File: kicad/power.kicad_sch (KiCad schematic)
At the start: 6 parts, among them J1 Bus_PCI_Express_x1, J6 USB_C_Receptacle_USB2.0_16P

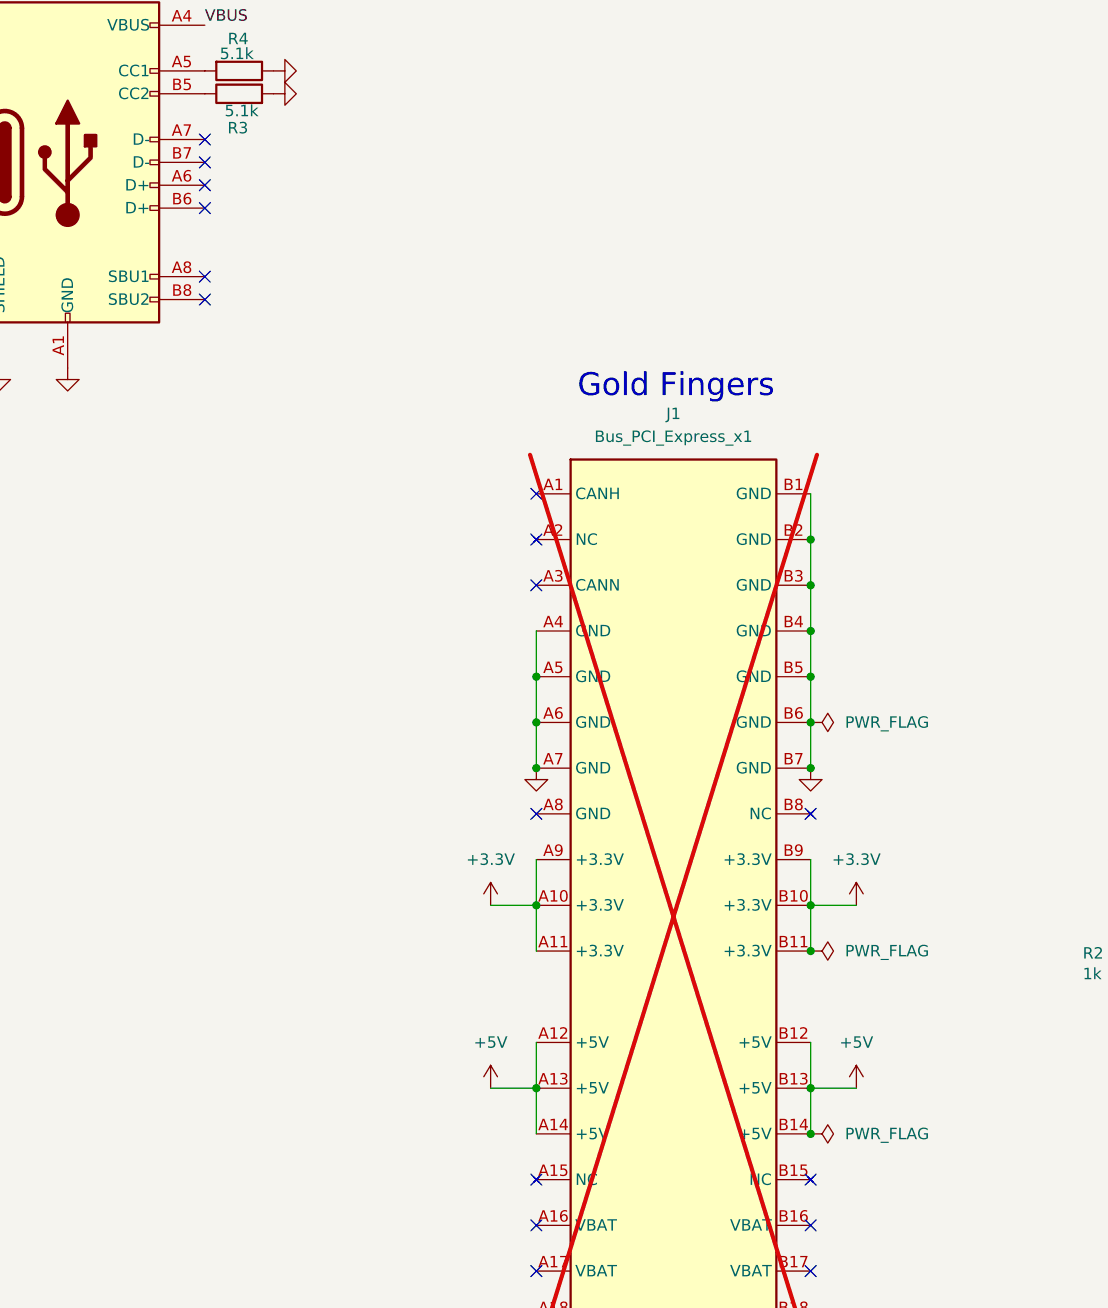
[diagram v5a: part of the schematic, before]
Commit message: update symbol data fields, add lcsc PN and links
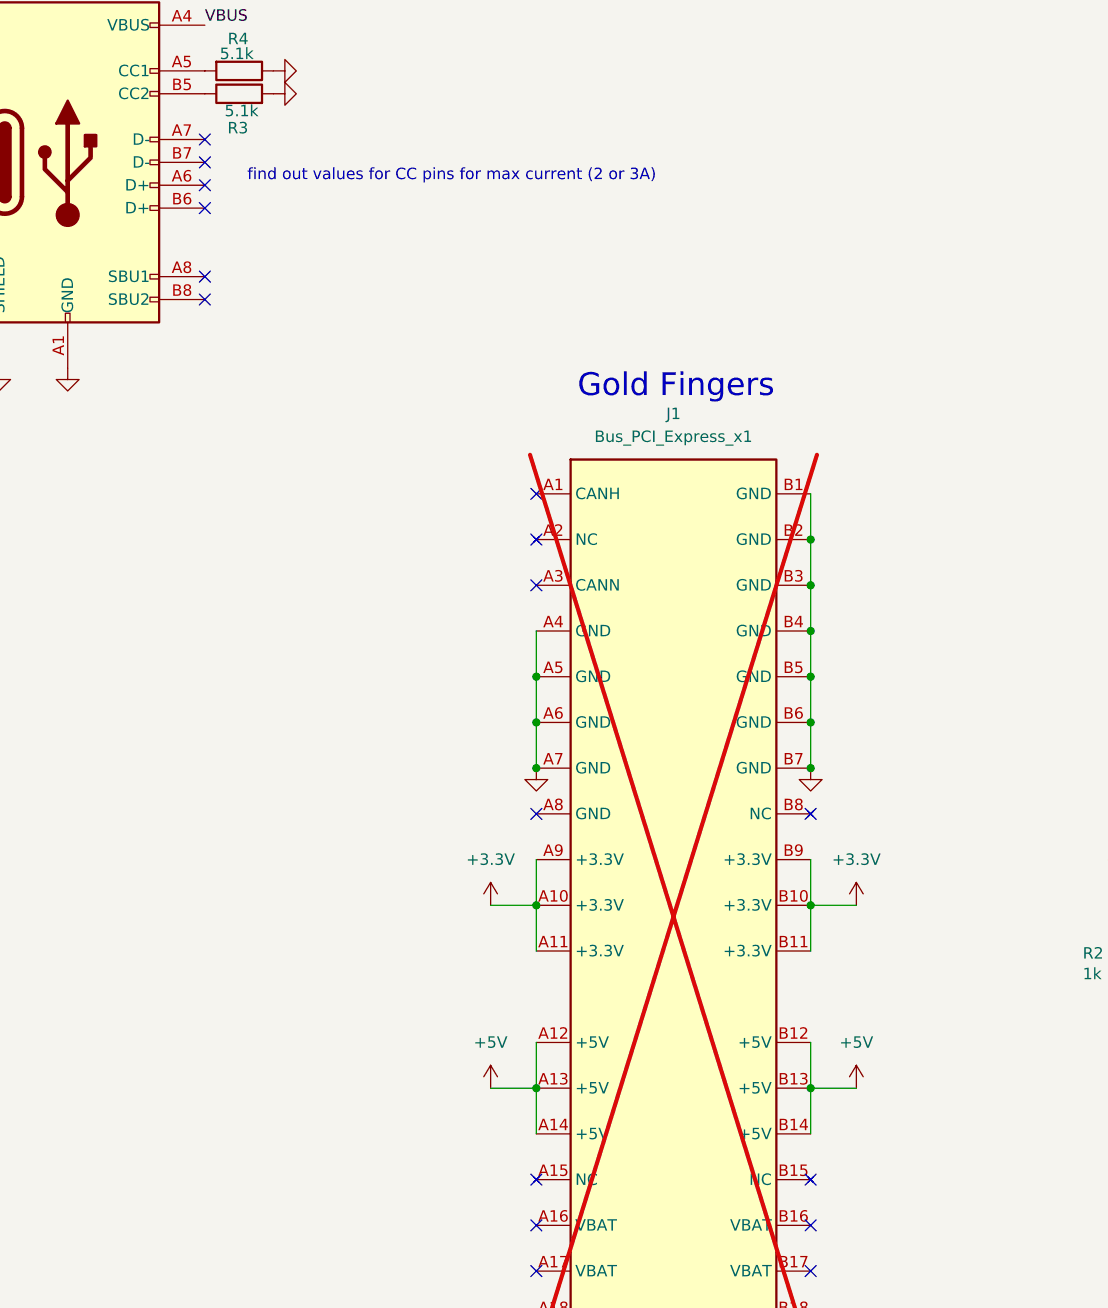
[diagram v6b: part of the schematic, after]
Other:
- note added: "find out values for CC pins for max current (2 or 3A)"

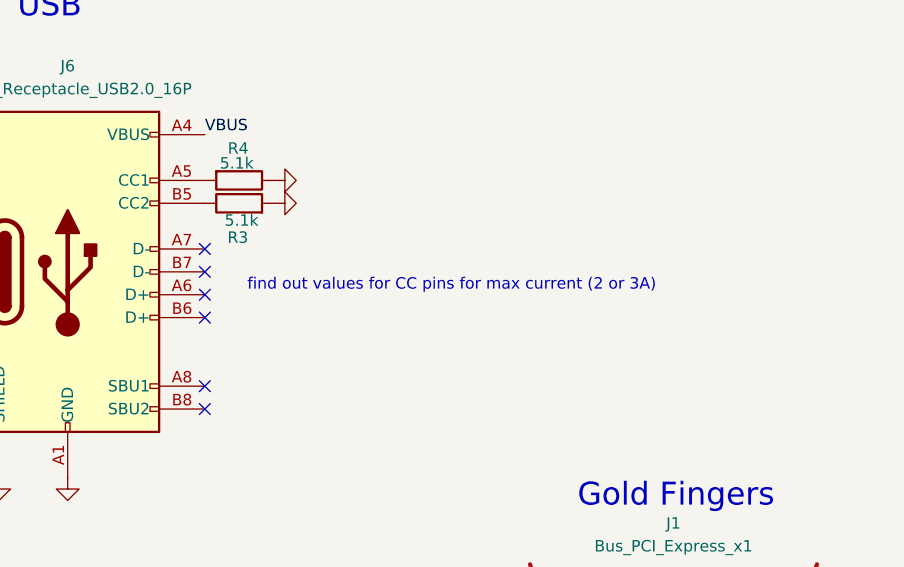
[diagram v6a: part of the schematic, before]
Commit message: delete old buck, replace with buck/boost
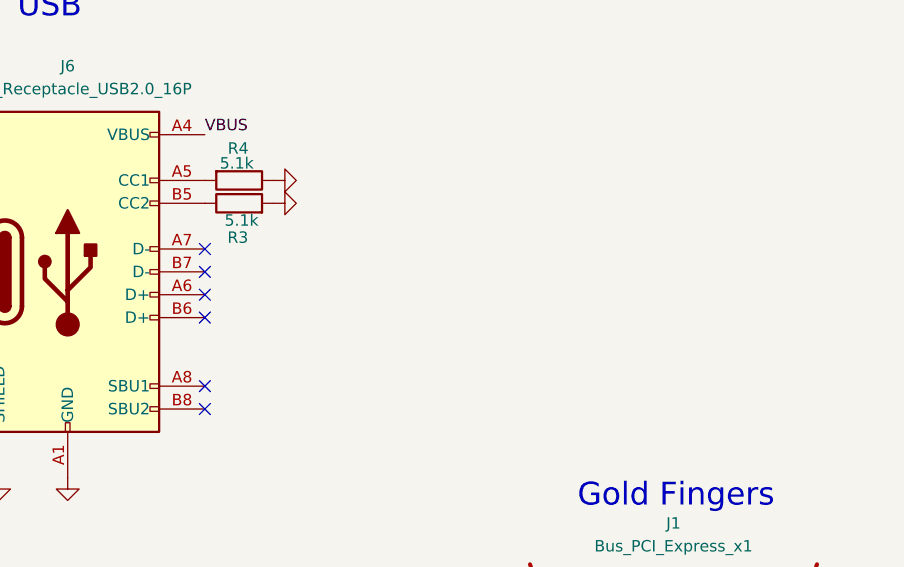
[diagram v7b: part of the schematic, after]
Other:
- note removed: "find out values for CC pins for max current (2 or 3A)"
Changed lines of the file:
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@@
-		)
-	)
-	(text "find out values for CC pins for max current (2 or 3A)"
-		(exclude_from_sim no)
-		(at 82.042 54.864 0)
-		(effects
-			(font
-				(size 1.27 1.27)
-			)
 		)
 	)

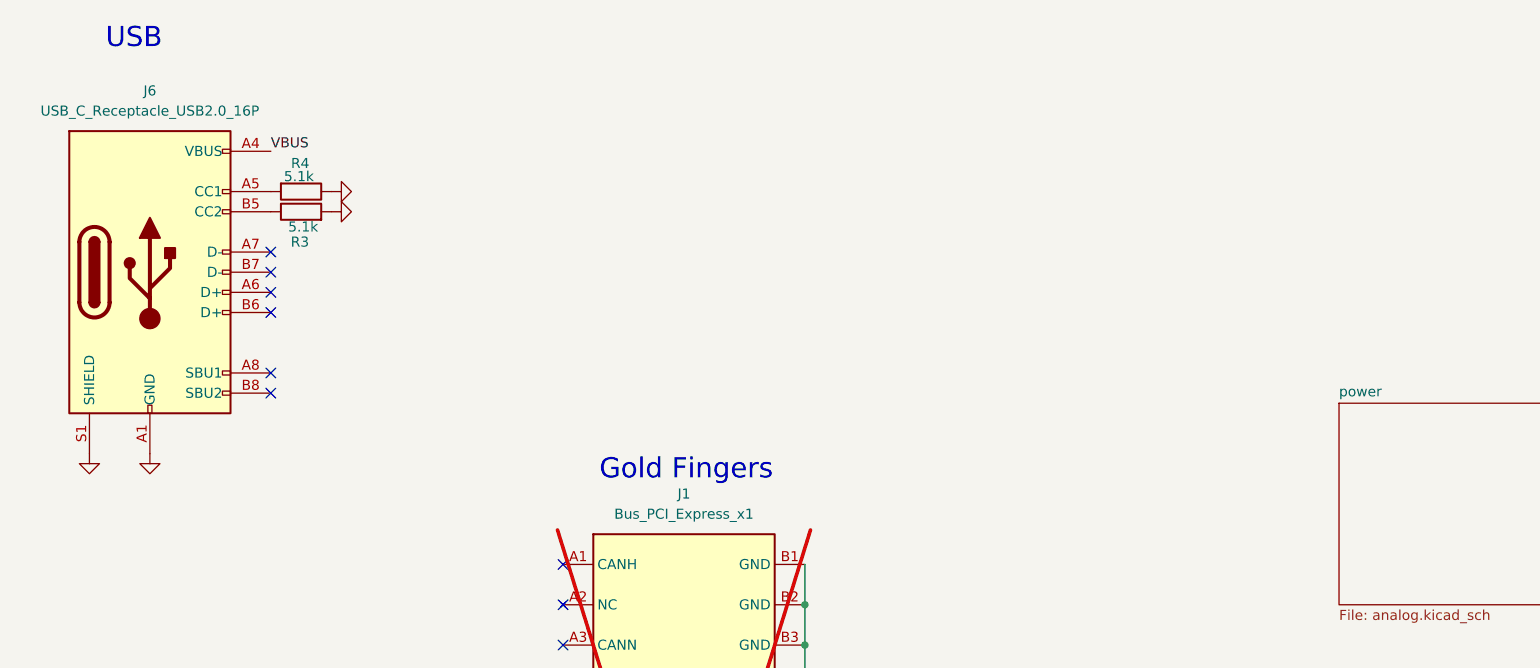
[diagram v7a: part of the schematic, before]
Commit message: add 5v buck-boost schematic
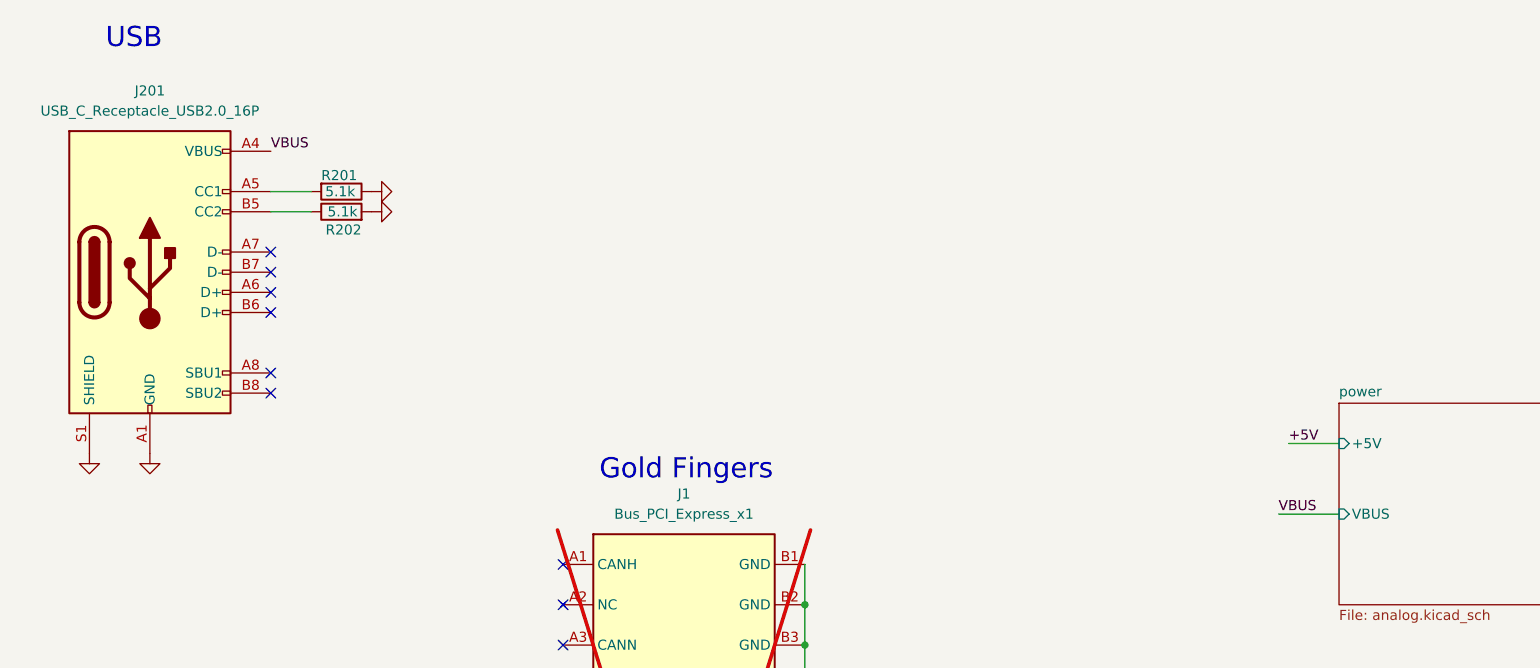
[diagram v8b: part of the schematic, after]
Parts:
- renumbered J6 to J201, R4 to R201, R3 to R202
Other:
- sheet power ports: added +5V, VBUS; removed none
- moved on the sheet: R201, R202
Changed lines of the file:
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@@
+	(wire
+		(pts
+			(xy 59.69 43.18) (xy 54.61 43.18)
+		)
+		(stroke
+			(width 0)
+			(type default)
+		)
+	)
 	(wire
 		(pts
@@
 	(wire
 		(pts
+			(xy 181.61 83.82) (xy 189.23 83.82)
+		)
+		(stroke
+			(width 0)
+			(type default)
+		)
+	)
+	(wire
+		(pts
 			(xy 86.36 135.89) (xy 91.44 135.89)
 		)
@@
 	(wire
 		(pts
+			(xy 182.88 74.93) (xy 189.23 74.93)
+		)
+		(stroke
+			(width 0)
+			(type default)
+		)
+	)
+	(wire
+		(pts
 			(xy 91.44 115.57) (xy 91.44 120.65)
 		)
@@
 	(wire
 		(pts
+			(xy 59.69 45.72) (xy 54.61 45.72)
+		)
+		(stroke
+			(width 0)
+			(type default)
+		)
+	)
+	(wire
+		(pts
 			(xy 91.44 156.21) (xy 91.44 151.13)
 		)
@@
 			(width 0)
 			(type default)
+		)
+	)
+	(label "+5V"
+		(at 182.88 74.93 0)
+		(effects
+			(font
+				(size 1.27 1.27)
+			)
+			(justify left bottom)
 		)
 	)
 	(label "VBUS"
 		(at 54.61 38.1 0)
+		(effects
+			(font
+				(size 1.27 1.27)
+			)
+			(justify left bottom)
+		)
+	)
+	(label "VBUS"
+		(at 181.61 83.82 0)
 		(effects
 			(font
@@
 	(symbol
 		(lib_id "power:GND")
-		(at 62.23 45.72 90)
+		(at 67.31 45.72 90)
 		(unit 1)
 		(exclude_from_sim no)
@@
 		(fields_autoplaced yes)
 		(property "Reference" "#PWR019"
-			(at 68.58 45.72 0)
+			(at 73.66 45.72 0)
 			(effects
 				(font
@@
 		)
 		(property "Value" "GND"
+			(at 72.39 45.72 0)
+			(effects
+				(font
+					(size 1.27 1.27)
+				)
+				(hide yes)
+			)
+		)
+		(property "Footprint" ""
 			(at 67.31 45.72 0)
 			(effects
@@
 			)
 		)
-		(property "Footprint" ""
-			(at 62.23 45.72 0)
-			(effects
-				(font
-					(size 1.27 1.27)
-				)
-				(hide yes)
-			)
-		)
 		(property "Datasheet" ""
-			(at 62.23 45.72 0)
+			(at 67.31 45.72 0)
 			(effects
 				(font
@@
 		)
 		(property "Description" "Power symbol creates a global label with name \"GND\" , ground"
-			(at 62.23 45.72 0)
+			(at 67.31 45.72 0)
 			(effects
 				(font
@@
 	(symbol
 		(lib_id "power:GND")
-		(at 62.23 43.18 90)
+		(at 67.31 43.18 90)
 		(unit 1)
 		(exclude_from_sim no)
@@
 		(fields_autoplaced yes)
 		(property "Reference" "#PWR020"
-			(at 68.58 43.18 0)
+			(at 73.66 43.18 0)
 			(effects
 				(font
@@
 		)
 		(property "Value" "GND"
+			(at 72.39 43.18 0)
+			(effects
+				(font
+					(size 1.27 1.27)
+				)
+				(hide yes)
+			)
+		)
+		(property "Footprint" ""
 			(at 67.31 43.18 0)
 			(effects
@@
 			)
 		)
-		(property "Footprint" ""
-			(at 62.23 43.18 0)
-			(effects
-				(font
-					(size 1.27 1.27)
-				)
-				(hide yes)
-			)
-		)
 		(property "Datasheet" ""
-			(at 62.23 43.18 0)
+			(at 67.31 43.18 0)
 			(effects
 				(font
@@
 		)
 		(property "Description" "Power symbol creates a global label with name \"GND\" , ground"
-			(at 62.23 43.18 0)
+			(at 67.31 43.18 0)
 			(effects
 				(font
@@
 	(symbol
 		(lib_id "Device:R")
-		(at 58.42 45.72 90)
+		(at 63.5 45.72 90)
 		(unit 1)
 		(exclude_from_sim no)
@@
 		(on_board yes)
 		(dnp no)
-		(property "Reference" "R3"
-			(at 59.436 49.53 90)
+		(property "Reference" "R202"
+			(at 66.04 48.006 90)
 			(effects
 				(font
@@
 		)
 		(property "Value" "5.1k"
-			(at 60.579 47.625 90)
+			(at 65.532 45.72 90)
 			(effects
 				(font
@@
 		)
 		(property "Footprint" "Resistor_SMD:R_0402_1005Metric"
-			(at 58.42 47.498 90)
+			(at 63.5 47.498 90)
 			(effects
 				(font
@@
 		)
 		(property "Datasheet" "~"
-			(at 58.42 45.72 0)
+			(at 63.5 45.72 0)
 			(effects
 				(font
@@
 		)
 		(property "Description" "Resistor"
-			(at 58.42 45.72 0)
+			(at 63.5 45.72 0)
 			(effects
 				(font
@@
 		)
 		(property "JLC Link" "https://jlcpcb.com/partdetail/26648-0402WGF5101TCE/C25905"
-			(at 58.42 45.72 0)
+			(at 63.5 45.72 0)
 			(effects
 				(font
@@
 		)
 		(property "basic?" "yes"
-			(at 58.42 45.72 0)
+			(at 63.5 45.72 0)
 			(effects
 				(font
@@
 		)
 		(property "info" "5.1k ohm"
-			(at 58.42 45.72 0)
+			(at 63.5 45.72 0)
 			(effects
 				(font
@@
 		)
 		(property "price" "C$0.0006"
-			(at 58.42 45.72 0)
+			(at 63.5 45.72 0)
 			(effects
 				(font
@@
 		)
 		(property "notes" ""
-			(at 58.42 45.72 0)
+			(at 63.5 45.72 0)
 			(effects
 				(font
@@
 		)
 		(property "LCSC PN" "C25905"
-			(at 58.42 45.72 0)
+			(at 63.5 45.72 0)
 			(effects
 				(font
@@
 		)
 		(property "Package" ""
-			(at 58.42 45.72 90)
+			(at 63.5 45.72 90)
 			(effects
 				(font
@@
 		)
 		(property "Comment" ""
-			(at 58.42 45.72 90)
+			(at 63.5 45.72 90)
 			(effects
 				(font
@@
 		)
 		(property "Current Draw" ""
-			(at 58.42 45.72 90)
+			(at 63.5 45.72 90)
 			(effects
 				(font
@@
 		)
 		(property "TYPE" ""
-			(at 58.42 45.72 90)
+			(at 63.5 45.72 90)
 			(effects
 				(font
@@
 			(project "sensors"
 				(path "/612ece3f-e722-4b33-8111-645d24cfcf05"
-					(reference "R3")
+					(reference "R202")
 					(unit 1)
 				)
@@
 	(symbol
 		(lib_id "Device:R")
-		(at 58.42 43.18 270)
+		(at 63.5 43.18 270)
 		(unit 1)
 		(exclude_from_sim no)
@@
 		(on_board yes)
 		(dnp no)
-		(property "Reference" "R4"
-			(at 57.15 39.624 90)
+		(property "Reference" "R201"
+			(at 60.96 41.148 90)
 			(effects
 				(font
@@
 		)
 		(property "Value" "5.1k"
-			(at 56.261 41.275 90)
+			(at 61.468 43.18 90)
 			(effects
 				(font
@@
 		)
 		(property "Footprint" "Resistor_SMD:R_0402_1005Metric"
-			(at 58.42 41.402 90)
+			(at 63.5 41.402 90)
 			(effects
 				(font
@@
 		)
 		(property "Datasheet" "~"
-			(at 58.42 43.18 0)
+			(at 63.5 43.18 0)
 			(effects
 				(font
@@
 		)
 		(property "Description" "Resistor"
-			(at 58.42 43.18 0)
+			(at 63.5 43.18 0)
 			(effects
 				(font
@@
 		)
 		(property "JLC Link" "https://jlcpcb.com/partdetail/26648-0402WGF5101TCE/C25905"
-			(at 58.42 43.18 0)
+			(at 63.5 43.18 0)
 			(effects
 				(font
@@
 		)
 		(property "basic?" "yes"
-			(at 58.42 43.18 0)
+			(at 63.5 43.18 0)
 			(effects
 				(font
@@
 		)
 		(property "info" "5.1k ohm"
-			(at 58.42 43.18 0)
+			(at 63.5 43.18 0)
 			(effects
 				(font
@@
 		)
 		(property "price" "C$0.0006"
-			(at 58.42 43.18 0)
+			(at 63.5 43.18 0)
 			(effects
 				(font
@@
 		)
 		(property "notes" ""
-			(at 58.42 43.18 0)
+			(at 63.5 43.18 0)
 			(effects
 				(font
@@
 		)
 		(property "LCSC PN" "C25905"
-			(at 58.42 43.18 0)
+			(at 63.5 43.18 0)
 			(effects
 				(font
@@
 		)
 		(property "Package" ""
-			(at 58.42 43.18 90)
+			(at 63.5 43.18 90)
 			(effects
 				(font
@@
 		)
 		(property "Comment" ""
-			(at 58.42 43.18 90)
+			(at 63.5 43.18 90)
 			(effects
 				(font
@@
 		)
 		(property "Current Draw" ""
-			(at 58.42 43.18 90)
+			(at 63.5 43.18 90)
 			(effects
 				(font
@@
 		)
 		(property "TYPE" ""
-			(at 58.42 43.18 90)
+			(at 63.5 43.18 90)
 			(effects
 				(font
@@
 			(project "sensors"
 				(path "/612ece3f-e722-4b33-8111-645d24cfcf05"
-					(reference "R4")
+					(reference "R201")
 					(unit 1)
 				)
@@
 		(dnp no)
 		(fields_autoplaced yes)
-		(property "Reference" "J6"
+		(property "Reference" "J201"
 			(at 39.37 30.48 0)
 			(effects
@@
 			(project ""
 				(path "/612ece3f-e722-4b33-8111-645d24cfcf05"
-					(reference "J6")
+					(reference "J201")
 					(unit 1)
 				)
@@
 			)
 		)
+		(pin "VBUS" input
+			(at 189.23 83.82 180)
+			(effects
+				(font
+					(size 1.27 1.27)
+				)
+				(justify left)
+			)
+		)
+		(pin "+5V" input
+			(at 189.23 74.93 180)
+			(effects
+				(font
+					(size 1.27 1.27)
+				)
+				(justify left)
+			)
+		)
